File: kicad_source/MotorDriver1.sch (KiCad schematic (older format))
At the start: 25 parts, among them CN10 691322310004, CN11 BM05B-SRSS-TB, U2 TMC5130A-TA

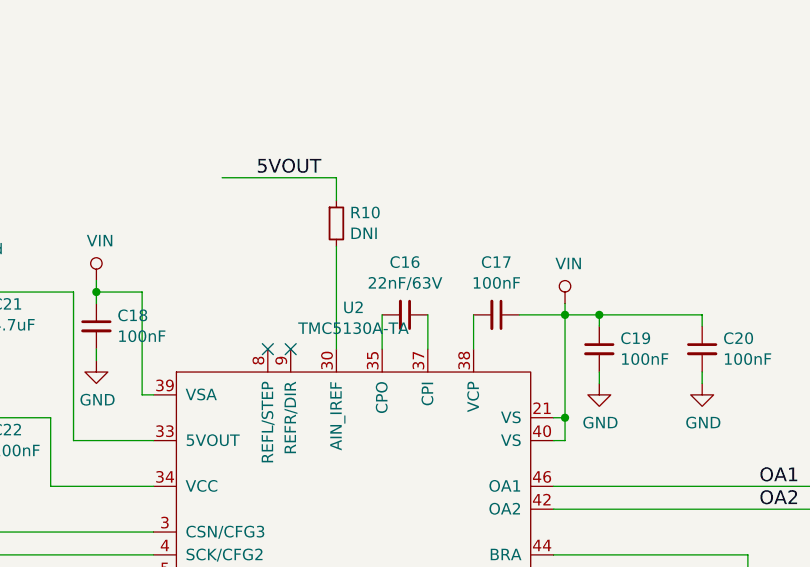
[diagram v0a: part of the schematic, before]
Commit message: updated part numbers
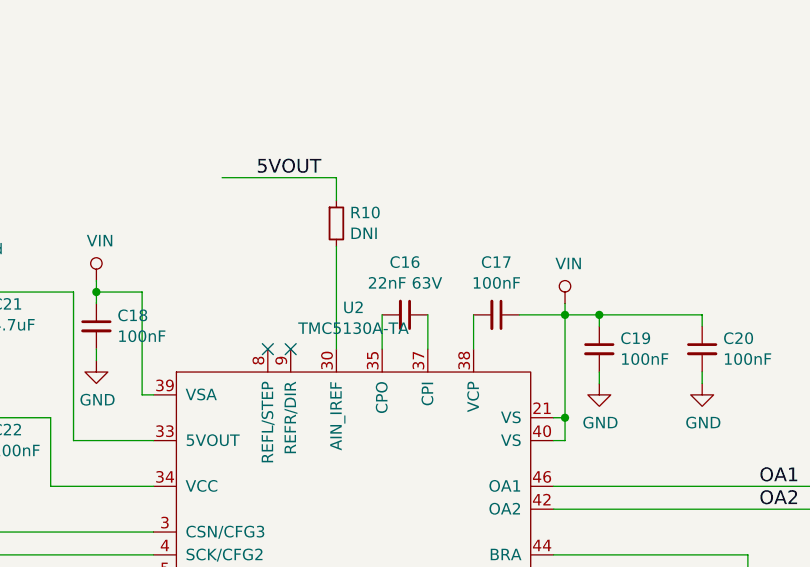
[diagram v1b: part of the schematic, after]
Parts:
- C16: value 22nF/63V -> 22nF 63V
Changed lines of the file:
@@
 P 6150 1900
 F 0 "C16" V 5921 1900 50  0000 C CNN
-F 1 "22nF/63V" V 6012 1900 50  0000 C CNN
+F 1 "22nF 63V" V 6012 1900 50  0000 C CNN
 F 2 "capacitors:C_0603" H 6150 1750 50  0001 C CNN
 F 3 "" H 6150 1900 50  0000 C CNN

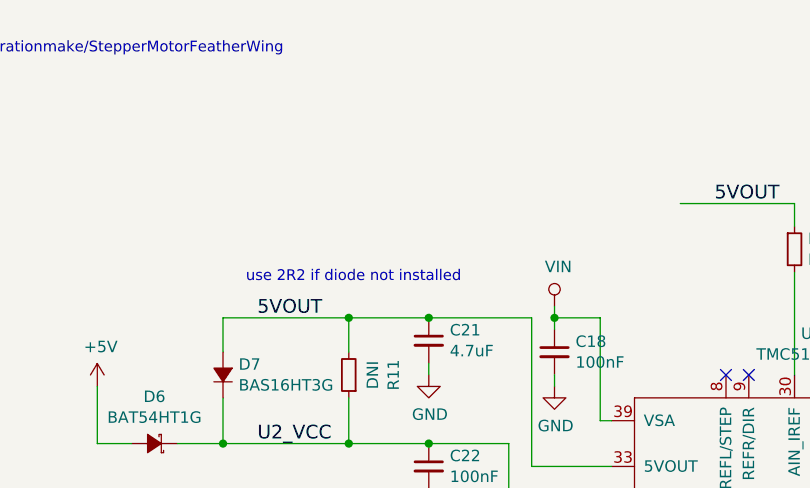
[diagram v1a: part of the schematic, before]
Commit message: corrected position of mounting holes for heat spreader, added information on input voltage
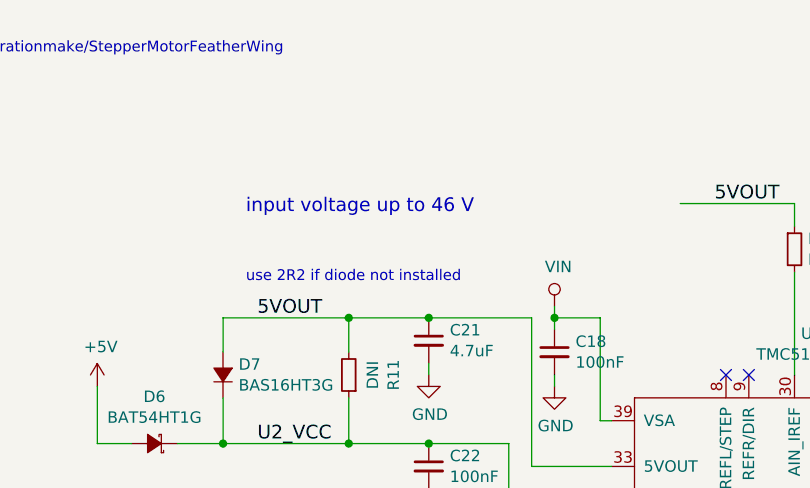
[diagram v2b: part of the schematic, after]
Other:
- note added: "input voltage up to 46 V"
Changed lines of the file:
@@
 Wire Wire Line
 	8400 3000 8400 3250
+Text Notes 3450 1350 0    60   ~ 0
+input voltage up to 46 V
 $EndSCHEMATC

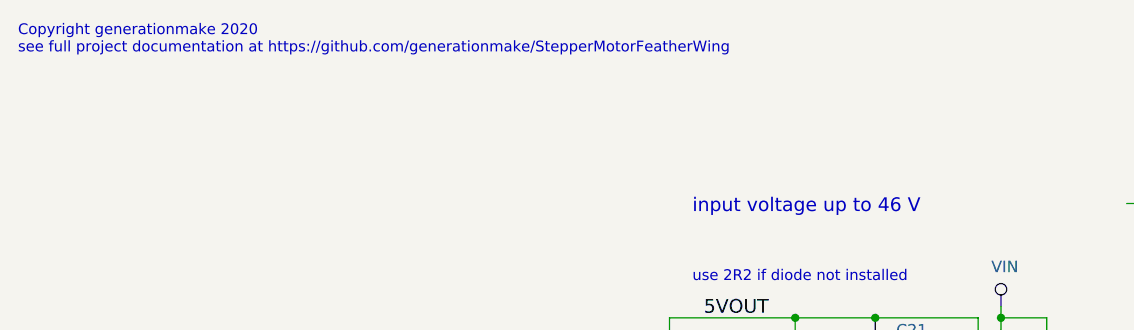
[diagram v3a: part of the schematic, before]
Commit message: corrected links and titles, generated schematic pdf and net list
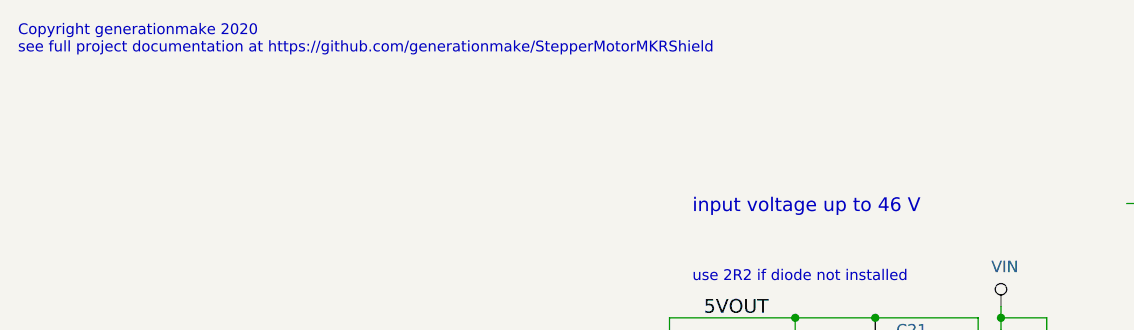
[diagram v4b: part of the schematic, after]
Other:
- note added: "Copyright generationmake 2020\nsee full project documentation at https://github.com/generationmake/StepperMotorMKRShield"
- note removed: "Copyright generationmake 2020\nsee full project documentation at https://github.com/generationmake/StepperMotorFeatherWing"
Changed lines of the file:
@@
 encoding utf-8
 Sheet 4 6
-Title "StepperMotorFeatherWing"
-Date "2020-07-11"
+Title "StepperMotorMKRShield"
+Date "2020-07-12"
 Rev "1.1"
 Comp "generationmake"
@@
 $EndDescr
 Text Notes 500  650  0    47   ~ 0
-Copyright generationmake 2020\nsee full project documentation at https://github.com/generationmake/StepperMotorFeatherWing
+Copyright generationmake 2020\nsee full project documentation at https://github.com/generationmake/StepperMotorMKRShield
 Text Notes 7000 6900 0    43   ~ 0
 You may redistribute and modify this documentation under the terms of the CERN OHL v.1.2. (http://ohwr.org/cernohl). \nThis documentation is distributed WITHOUT ANY EXPRESS OR IMPLIED WARRANTY, INCLUDING OF MERCHANTABILITY, SATISFACTORY \nQUALITY AND FITNESS FOR A PARTICULAR PURPOSE. Please see the CERN OHL v.1.2  for applicable conditions
